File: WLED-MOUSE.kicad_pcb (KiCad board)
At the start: 2 copper layers, 16 parts, among them J1 FTDI-header, J2 Power-in, J4 Pixel-strip, J6 Pixel-strip, J7 Pixel-strip, J8 Pixel-strip, SW1 SW_MEC_5E, SW2 SW_MEC_5E, U1 ESP32-WROOM-32D, U2 ESP32-WROOM-32D, U3 SN74LV4T125

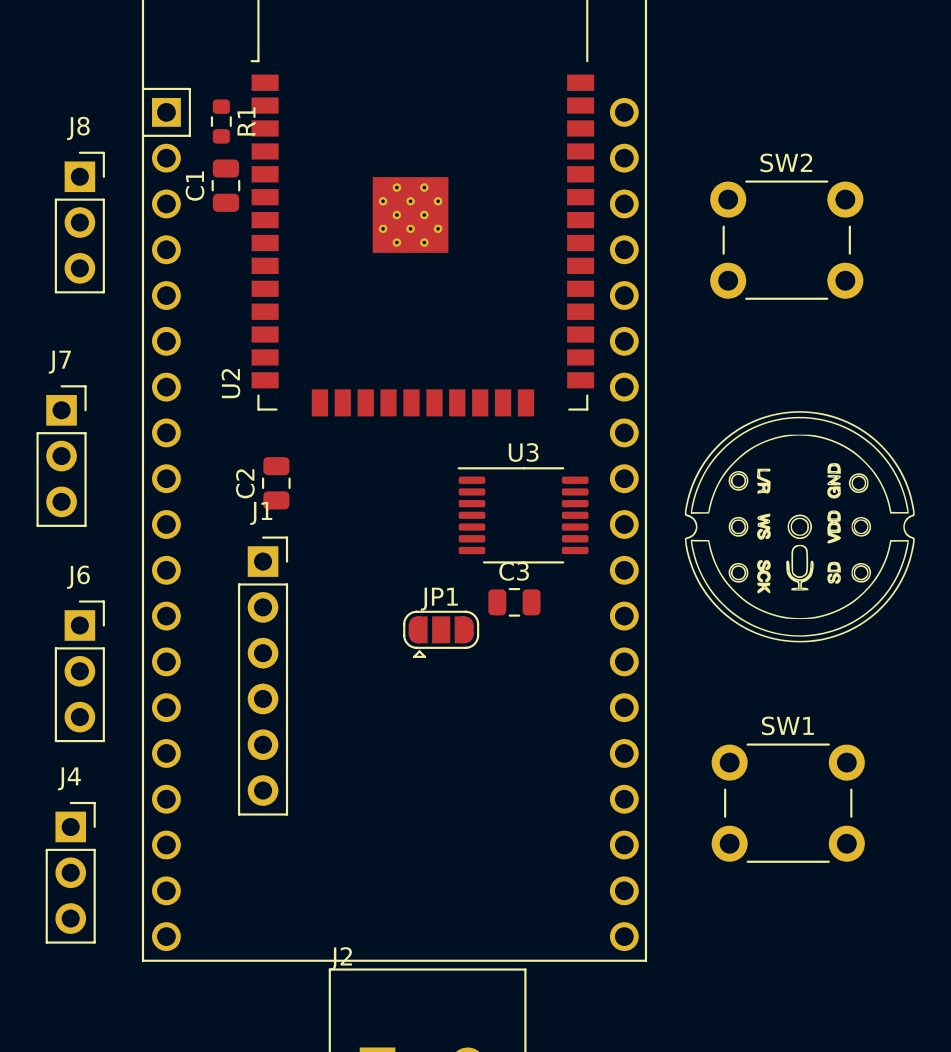
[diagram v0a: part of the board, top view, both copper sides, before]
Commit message: added the JLC PCB rules and settings, for eventual prodcution, also tried to add some of the stuff for the mic.
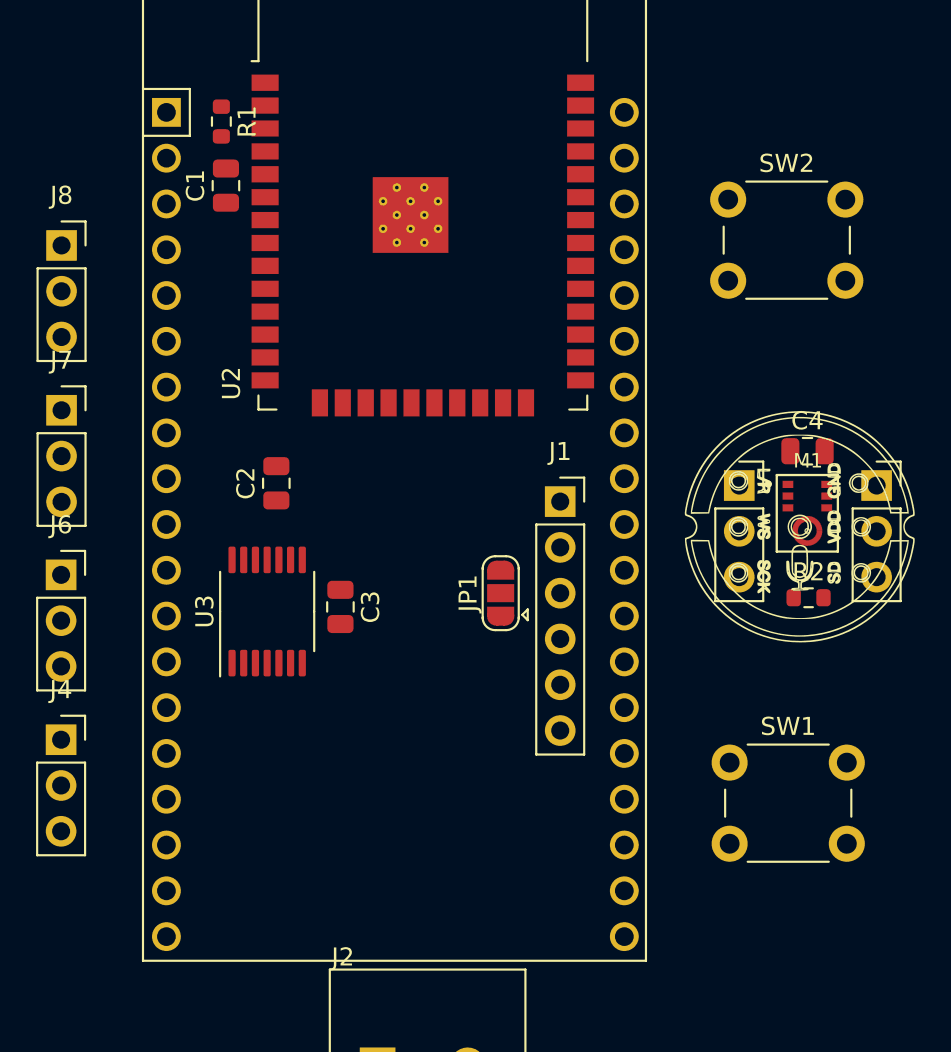
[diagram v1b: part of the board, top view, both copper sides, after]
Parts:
- added C4: C, Capacitor_SMD:C_0805_2012Metric, F.Cu at (203.7, 101.6)
- added J3: Conn_01x03_Female, Connector_PinSocket_2.54mm:PinSocket_1x03_P2.54mm_Vertical, F.Cu at (207.5, 103.5)
- added J5: Conn_01x03_Female, Connector_PinSocket_2.54mm:PinSocket_1x03_P2.54mm_Vertical, F.Cu at (199.9, 103.5)
- added M1: INMP441, mic:MIC_DMM-4026-B-I2S-R, F.Cu at (203.7, 105.0)
- added R2: R, Resistor_SMD:R_0603_1608Metric, F.Cu at (203.8, 109.7)
- moved J1 16.8 mm to (190.0, 104.4)
- moved U3 15.2 mm to (173.7, 110.5), turned to 90 degrees
- moved C3 9.66 mm to (177.8, 110.2), turned to -90 degrees
- moved J4 4.87 mm to (162.3, 117.6)
- moved J8 3.94 mm to (162.3, 90.2)
- moved JP1 3.88 mm to (186.7, 109.5), turned to 90 degrees
- moved J6 3.00 mm to (162.3, 108.5)
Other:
- copper layers 2 -> 4

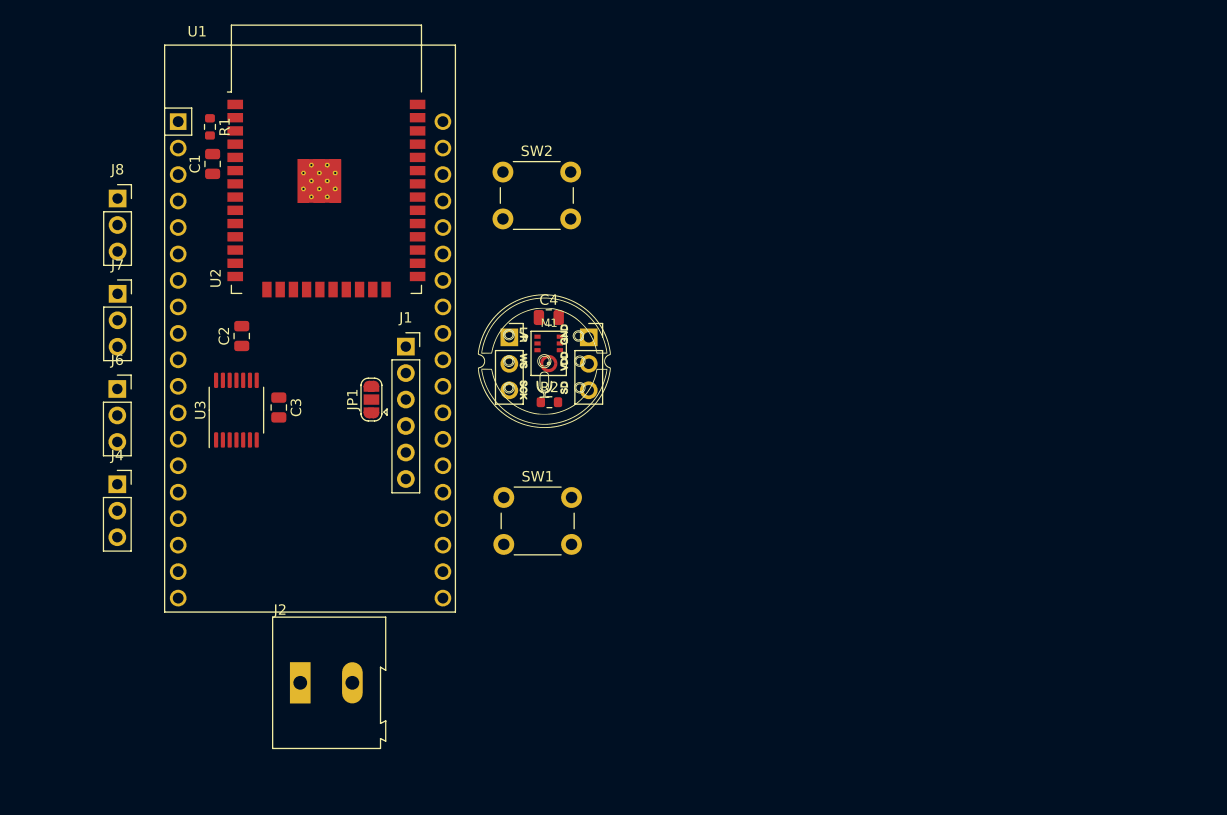
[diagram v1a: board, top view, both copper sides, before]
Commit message: added footprint for the thought hole mic board, thing?
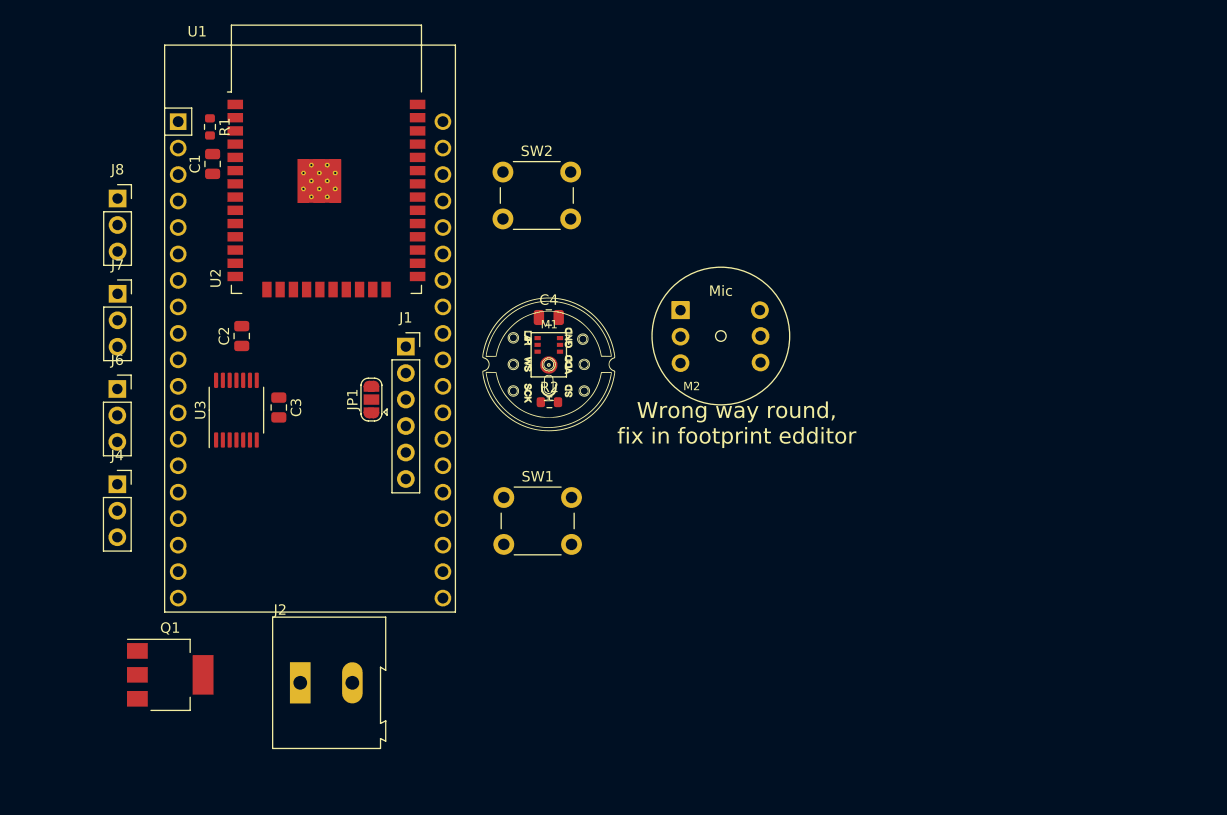
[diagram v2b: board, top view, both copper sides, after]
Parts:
- removed J3, J5: Conn_01x03_Female, Connector_PinSocket_2.54mm:PinSocket_1x03_P2.54mm_Vertical
- added M2: INMP441-TH, mic:MIC_DMM-4026-B-I2S-R-TH, F.Cu at (220.2, 103.4)
- added Q1: NDT3055L, Package_TO_SOT_SMD:SOT-223-3_TabPin2, F.Cu at (167.4, 135.9)
- moved M1 0.14 mm to (203.7, 105.2)
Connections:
- J4 pad 1: GND -> Net-(J4-Pad1)
- J6 pad 1: GND -> Net-(J4-Pad1)
- J7 pad 1: GND -> Net-(J4-Pad1)
- J8 pad 1: GND -> Net-(J4-Pad1)
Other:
- board text added: "Wrong way round, fix in footprint edditor"

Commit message: started doing some more layout
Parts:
- removed Q1: NDT3055L, Package_TO_SOT_SMD:SOT-223-3_TabPin2
- moved M2 16.8 mm to (203.7, 106.2)
- moved J2 10.9 mm to (168.9, 137.4)
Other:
- board outline added: 54.4 x 67.6 mm
- board text removed: "Wrong way round, fix in footprint edditor"
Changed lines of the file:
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@@
   (net 68 "Net-(M1-Pad8)")
   (net 69 "Net-(J4-Pad1)")
-  (net 70 "unconnected-(Q1-Pad1)")
-  (net 71 "unconnected-(Q1-Pad2)")
-  (net 72 "unconnected-(Q1-Pad3)")
   (footprint "Capacitor_SMD:C_0805_2012Metric" (layer "F.Cu")
     (at 203.708 101.6)
@@
     )
   )
-  (footprint "Package_TO_SOT_SMD:SOT-223-3_TabPin2" (layer "F.Cu")
-    (at 167.386 135.89)
-    (descr "module CMS SOT223 4 pins")
-    (tags "CMS SOT")
-    (property "Sheetfile" "WLED-MOUSE.kicad_sch")
-    (property "Sheetname" "")
-    (attr smd)
-    (fp_text reference "Q1" (at 0 -4.5) (layer "F.SilkS")
-      (effects (font (size 1 1) (thickness 0.15)))
-    )
-    (fp_text value "NDT3055L" (at 0 4.5) (layer "F.Fab")
-      (effects (font (size 1 1) (thickness 0.15)))
-    )
-    (fp_text user "${REFERENCE}" (at 0 0 90) (layer "F.Fab")
-      (effects (font (size 0.8 0.8) (thickness 0.12)))
-    )
-    (fp_line (start -1.85 3.41) (end 1.91 3.41) (layer "F.SilkS") (width 0.12))
-    (fp_line (start 1.91 3.41) (end 1.91 2.15) (layer "F.SilkS") (width 0.12))
-    (fp_line (start 1.91 -3.41) (end 1.91 -2.15) (layer "F.SilkS") (width 0.12))
-    (fp_line (start -4.1 -3.41) (end 1.91 -3.41) (layer "F.SilkS") (width 0.12))
-    (fp_line (start 4.4 -3.6) (end -4.4 -3.6) (layer "F.CrtYd") (width 0.05))
-    (fp_line (start -4.4 -3.6) (end -4.4 3.6) (layer "F.CrtYd") (width 0.05))
-    (fp_line (start 4.4 3.6) (end 4.4 -3.6) (layer "F.CrtYd") (width 0.05))
-    (fp_line (start -4.4 3.6) (end 4.4 3.6) (layer "F.CrtYd") (width 0.05))
-    (fp_line (start 1.85 -3.35) (end 1.85 3.35) (layer "F.Fab") (width 0.1))
-    (fp_line (start -1.85 -2.35) (end -0.85 -3.35) (layer "F.Fab") (width 0.1))
-    (fp_line (start -1.85 3.35) (end 1.85 3.35) (layer "F.Fab") (width 0.1))
-    (fp_line (start -0.85 -3.35) (end 1.85 -3.35) (layer "F.Fab") (width 0.1))
-    (fp_line (start -1.85 -2.35) (end -1.85 3.35) (layer "F.Fab") (width 0.1))
-    (pad "1" smd rect (at -3.15 -2.3) (size 2 1.5) (layers "F.Cu" "F.Paste" "F.Mask")
-      (net 70 "unconnected-(Q1-Pad1)") (pinfunction "G") (pintype "input"))
-    (pad "2" smd rect (at -3.15 0) (size 2 1.5) (layers "F.Cu" "F.Paste" "F.Mask")
-      (net 71 "unconnected-(Q1-Pad2)") (pinfunction "D") (pintype "passive"))
-    (pad "2" smd rect (at 3.15 0) (size 2 3.8) (layers "F.Cu" "F.Paste" "F.Mask")
-      (net 71 "unconnected-(Q1-Pad2)") (pinfunction "D") (pintype "passive"))
-    (pad "3" smd rect (at -3.15 2.3) (size 2 1.5) (layers "F.Cu" "F.Paste" "F.Mask")
-      (net 72 "unconnected-(Q1-Pad3)") (pinfunction "S") (pintype "passive"))
-    (model "${KICAD6_3DMODEL_DIR}/Package_TO_SOT_SMD.3dshapes/SOT-223.wrl"
-      (offset (xyz 0 0 0))
-      (scale (xyz 1 1 1))
-      (rotate (xyz 0 0 0))
-    )
-  )
   (footprint "RF_Module:ESP32-WROOM-32" (layer "F.Cu")
     (at 182.372 89.408)
@@
   )
   (footprint "mic:MIC_DMM-4026-B-I2S-R-TH" (layer "F.Cu")
-    (at 220.218 103.378)
+    (at 203.677424 106.172)
     (property "Sheetfile" "WLED-MOUSE.kicad_sch")
     (property "Sheetname" "")
@@
     (fp_circle (center 0 0) (end 6.604 0) (layer "B.SilkS") (width 0.12) (fill none))
     (fp_circle (center 0 0) (end 0.508 0) (layer "B.SilkS") (width 0.12) (fill none))
-    (fp_circle (center 0 0) (end 0 -6.604) (layer "F.SilkS") (width 0.12) (fill none))
     (fp_circle (center 0 0) (end 0 -0.508) (layer "F.SilkS") (width 0.12) (fill none))
-    (pad "1" thru_hole rect (at -3.87 -2.48) (size 1.7 1.7) (drill 1) (layers *.Cu *.Mask)
-      (net 2 "GND") (pinfunction "L/R") (pintype "input"))
-    (pad "1" thru_hole rect (at -3.87 -2.48 90) (size 1.7 1.7) (drill 1) (layers *.Cu *.Mask)
+    (fp_circle (center 0 0) (end 0 -6.604) (layer "F.SilkS") (width 0.12) (fill none))
+    (pad "1" thru_hole rect (at 3.75 -2.48 90) (size 1.7 1.7) (drill 1) (layers *.Cu *.Mask)
       (net 2 "GND") (pinfunction "L/R") (pintype "input"))
-    (pad "2" thru_hole oval (at -3.87 0.06) (size 1.7 1.7) (drill 1) (layers *.Cu *.Mask)
+    (pad "2" thru_hole oval (at 3.81 0) (size 1.7 1.7) (drill 1) (layers *.Cu *.Mask)
       (net 65 "/WS") (pinfunction "WS") (pintype "input"))
-    (pad "3" thru_hole oval (at -3.87 2.6) (size 1.7 1.7) (drill 1) (layers *.Cu *.Mask)
+    (pad "3" thru_hole oval (at 3.81 2.54) (size 1.7 1.7) (drill 1) (layers *.Cu *.Mask)
       (net 64 "/SCK") (pinfunction "SCK") (pintype "input"))
-    (pad "4" thru_hole oval (at 3.75 -2.48 90) (size 1.7 1.7) (drill 1) (layers *.Cu *.Mask)
+    (pad "4" thru_hole circle (at -3.87 -2.48 90) (size 1.7 1.7) (drill 1) (layers *.Cu *.Mask)
       (net 2 "GND") (pinfunction "GND") (pintype "power_in"))
-    (pad "5" thru_hole oval (at 3.81 0) (size 1.7 1.7) (drill 1) (layers *.Cu *.Mask)
+    (pad "5" thru_hole oval (at -3.87 0.06) (size 1.7 1.7) (drill 1) (layers *.Cu *.Mask)
       (net 3 "+3.3V") (pinfunction "Vcc") (pintype "power_in"))
-    (pad "6" thru_hole oval (at 3.81 2.54) (size 1.7 1.7) (drill 1) (layers *.Cu *.Mask)
+    (pad "6" thru_hole oval (at -3.87 2.6) (size 1.7 1.7) (drill 1) (layers *.Cu *.Mask)
       (net 63 "/SD") (pinfunction "SD") (pintype "input"))
   )
@@
     (property "Sheetname" "")
     (attr through_hole)
-    (fp_text reference "J6" (at 0 -2.77) (layer "F.SilkS")
+    (fp_text reference "J6" (at 0 -2.77) (layer "F.Fab")
       (effects (font (size 1 1) (thickness 0.15)))
     )
-    (fp_text value "Pixel-strip" (at 0 7.85) (layer "F.Fab")
+    (fp_text value "Pixel-strip" (at -3.302 2.54 90) (layer "F.SilkS")
       (effects (font (size 1 1) (thickness 0.15)))
     )
@@
     (property "Sheetname" "")
     (attr through_hole)
-    (fp_text reference "J4" (at 0 -2.77) (layer "F.SilkS")
+    (fp_text reference "J4" (at 0 -2.77) (layer "F.Fab")
       (effects (font (size 1 1) (thickness 0.15)))
     )
-    (fp_text value "Pixel-strip" (at 0 7.85) (layer "F.Fab")
+    (fp_text value "Pixel-strip" (at -3.302 2.286 90) (layer "F.SilkS")
       (effects (font (size 1 1) (thickness 0.15)))
     )
@@
   )
   (footprint "TerminalBlock:TerminalBlock_Altech_AK300-2_P5.00mm" (layer "F.Cu")
-    (at 179.861 136.652)
+    (at 168.939 137.414)
     (descr "Altech AK300 terminal block, pitch 5.0mm, 45 degree angled, see http://www.mouser.com/ds/2/16/PCBMETRC-24178.pdf")
     (tags "Altech AK300 terminal block pitch 5.0mm")
@@
     (property "Sheetname" "")
     (attr through_hole)
-    (fp_text reference "J2" (at -1.92 -6.99) (layer "F.SilkS")
+    (fp_text reference "J2" (at -1.92 -6.99) (layer "F.Fab")
       (effects (font (size 1 1) (thickness 0.15)))
     )
-    (fp_text value "Power-in" (at 2.78 7.75) (layer "F.Fab")
+    (fp_text value "Power-in" (at 2.78 7.75) (layer "F.SilkS")
       (effects (font (size 1 1) (thickness 0.15)))
     )
@@
     (property "Sheetname" "")
     (attr through_hole)
-    (fp_text reference "J8" (at 0 -2.77) (layer "F.SilkS")
+    (fp_text reference "J8" (at 0 -2.77) (layer "F.Fab")
       (effects (font (size 1 1) (thickness 0.15)))
     )
-    (fp_text value "Pixel-strip" (at 0 7.85) (layer "F.Fab")
+    (fp_text value "Pixel-strip" (at -3.327 2.525 90) (layer "F.SilkS")
       (effects (font (size 1 1) (thickness 0.15)))
     )
@@
     (property "Sheetname" "")
     (attr through_hole)
-    (fp_text reference "J1" (at 0 -2.77) (layer "F.SilkS")
+    (fp_text reference "J1" (at 0 -2.77) (layer "F.Fab")
       (effects (font (size 1 1) (thickness 0.15)))
     )
-    (fp_text value "FTDI-header" (at 0 15.47) (layer "F.Fab")
+    (fp_text value "FTDI-header" (at -3.048 12.954 90) (layer "F.SilkS")
       (effects (font (size 1 1) (thickness 0.15)))
     )
@@
     (property "Sheetname" "")
     (attr through_hole)
-    (fp_text reference "J7" (at 0 -2.77) (layer "F.SilkS")
+    (fp_text reference "J7" (at 0 -2.77) (layer "F.Fab")
       (effects (font (size 1 1) (thickness 0.15)))
     )
-    (fp_text value "Pixel-strip" (at 0 7.85) (layer "F.Fab")
+    (fp_text value "Pixel-strip" (at -3.327 2.779 90) (layer "F.SilkS")
       (effects (font (size 1 1) (thickness 0.15)))
     )
@@
       (xy 207.101492 108.108354)
     ) (layer "F.SilkS") (width 0) (fill solid))
-  (gr_text "Wrong way round, \nfix in footprint edditor\n" (at 221.742 111.76) (layer "F.SilkS")
-    (effects (font (size 1.524 1.524) (thickness 0.3048)))
-  )
+  (gr_poly
+    (pts
+      (xy 157.226 87.376)
+      (xy 164.846 79.756)
+      (xy 211.582 79.756)
+      (xy 211.582 134.366)
+      (xy 198.628 147.32)
+      (xy 157.226 147.32)
+    ) (layer "Edge.Cuts") (width 0.0381) (fill none))
   (group "" (id 20d868c9-54c9-4fa0-ad2a-ce6b30917857)
     (members

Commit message: checking its up to date,
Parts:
- moved C1 0.25 mm to (171.2, 86.9)
- moved R1 0.25 mm to (170.9, 83.3)
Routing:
- net Net-(J4-Pad1): track 0.00 -> 77.5 mm
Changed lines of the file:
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@@
   )
   (footprint "Resistor_SMD:R_0603_1608Metric" (layer "F.Cu")
-    (at 171.196 83.312 -90)
+    (at 170.942 83.312 -90)
     (descr "Resistor SMD 0603 (1608 Metric), square (rectangular) end terminal, IPC_7351 nominal, (Body size source: IPC-SM-782 page 72, https://www.pcb-3d.com/wordpress/wp-content/uploads/ipc-sm-782a_amendment_1_and_2.pdf), generated with kicad-footprint-generator")
     (tags "resistor")
@@
   )
   (footprint "Capacitor_SMD:C_0805_2012Metric" (layer "F.Cu")
-    (at 171.45 86.868 90)
+    (at 171.196 86.868 90)
     (descr "Capacitor SMD 0805 (2012 Metric), square (rectangular) end terminal, IPC_7351 nominal, (Body size source: IPC-SM-782 page 76, https://www.pcb-3d.com/wordpress/wp-content/uploads/ipc-sm-782a_amendment_1_and_2.pdf, https://docs.google.com/spreadsheets/d/1BsfQQcO9C6DZCsRaXUlFlo91Tg2WpOkGARC1WS5S8t0/edit?usp=sharing), generated with kicad-footprint-generator")
     (tags "capacitor")
@@
       (xy 157.226 147.32)
     ) (layer "Edge.Cuts") (width 0.0381) (fill none))
+  (segment (start 159.766 105.918) (end 159.766 105.41) (width 1) (layer "F.Cu") (net 69))
+  (segment (start 161.813 99.329) (end 159.766 97.282) (width 1) (layer "F.Cu") (net 69))
+  (segment (start 159.766 116.84) (end 159.766 105.41) (width 1) (layer "F.Cu") (net 69))
+  (segment (start 159.766 97.282) (end 159.766 91.186) (width 1) (layer "F.Cu") (net 69))
+  (segment (start 160.528 117.602) (end 159.766 116.84) (width 1) (layer "F.Cu") (net 69))
+  (segment (start 160.767 90.185) (end 162.331 90.185) (width 1) (layer "F.Cu") (net 69))
+  (segment (start 159.766 91.186) (end 160.767 90.185) (width 1) (layer "F.Cu") (net 69))
+  (segment (start 162.306 117.602) (end 160.528 117.602) (width 1) (layer "F.Cu") (net 69))
+  (segment (start 162.331 99.329) (end 161.813 99.329) (width 1) (layer "F.Cu") (net 69))
+  (segment (start 162.306 108.458) (end 159.766 105.918) (width 1) (layer "F.Cu") (net 69))
+  (segment (start 159.766 105.41) (end 159.766 97.282) (width 1) (layer "F.Cu") (net 69))
+  (segment (start 162.306 108.458) (end 159.766 105.918) (width 1) (layer "B.Cu") (net 69))
+  (segment (start 162.331 99.329) (end 161.813 99.329) (width 1) (layer "B.Cu") (net 69))
+  (segment (start 159.766 91.186) (end 160.767 90.185) (width 1) (layer "B.Cu") (net 69))
+  (segment (start 162.306 117.602) (end 160.528 117.602) (width 1) (layer "B.Cu") (net 69))
+  (segment (start 161.813 99.329) (end 159.766 97.282) (width 1) (layer "B.Cu") (net 69))
+  (segment (start 160.528 117.602) (end 159.766 116.84) (width 1) (layer "B.Cu") (net 69))
+  (segment (start 160.767 90.185) (end 162.331 90.185) (width 1) (layer "B.Cu") (net 69))
+  (segment (start 159.766 116.84) (end 159.766 91.186) (width 1) (layer "B.Cu") (net 69))
   (group "" (id 20d868c9-54c9-4fa0-ad2a-ce6b30917857)
     (members

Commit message: started some routing and layout stuff
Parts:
- moved C2 23.2 mm to (167.1, 81.3), turned to 0 degrees
- moved J1 16.0 mm to (202.7, 94.8)
- moved JP1 16.0 mm to (199.4, 99.8)
- moved R2 13.2 mm to (204.1, 122.9)
- moved C4 13.2 mm to (204.1, 114.7)
- moved M1 13.2 mm to (204.1, 118.3)
- moved M2 13.2 mm to (204.0, 119.3)
- moved J2 12.7 mm to (157.5, 131.8)
- moved SW1 9.75 mm to (200.5, 128.6)
- moved U1 5.03 mm to (168.1, 87.8)
- moved SW2 4.37 mm to (201.0, 83.6)
- moved C1 0.25 mm to (170.9, 86.9), turned to -90 degrees
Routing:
- net GND: track 0.00 -> 132.4 mm
- net /SCK: track 0.00 -> 80.4 mm, vias 0 -> 2
- net /SD: track 0.00 -> 62.0 mm
- net +5V: track 0.00 -> 46.2 mm
- net /WS: track 0.00 -> 42.1 mm, vias 0 -> 1
- net +3.3V: track 0.00 -> 37.6 mm
- net Net-(J8-Pad2): track 0.00 -> 26.2 mm, vias 0 -> 1
- net Net-(J7-Pad2): track 0.00 -> 21.6 mm, vias 0 -> 1
- net Net-(J6-Pad2): track 0.00 -> 16.4 mm, vias 0 -> 1
- net Net-(J4-Pad2): track 0.00 -> 15.4 mm, vias 0 -> 1
- net /Reset: track 0.00 -> 14.1 mm
- added copper zone on B.Cu, net GND
- added copper zone on F.Cu, net GND
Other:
- board size 54.4 x 67.6 mm -> 58.2 x 59.4 mm
